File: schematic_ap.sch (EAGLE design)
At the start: 25 parts, among them M1 WIRELESS-NRF24L01, U1 ATMEGA328P_TQFP, U3 MPU-6050

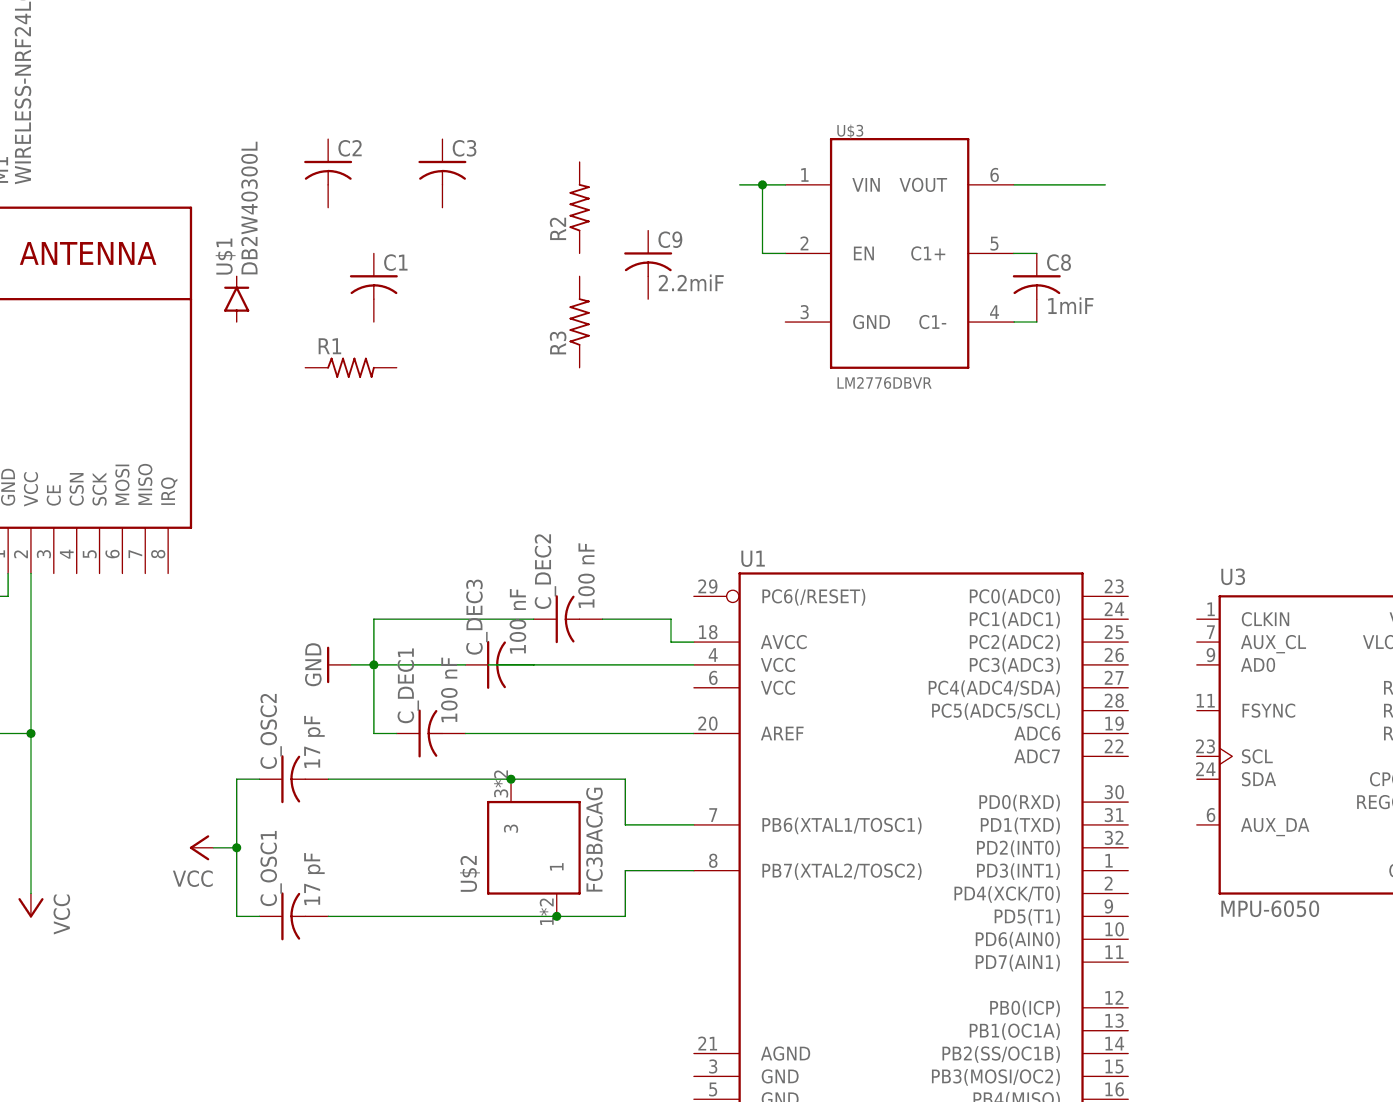
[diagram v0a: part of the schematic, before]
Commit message: New Oscillator
Added the 8MHZ Oscillator
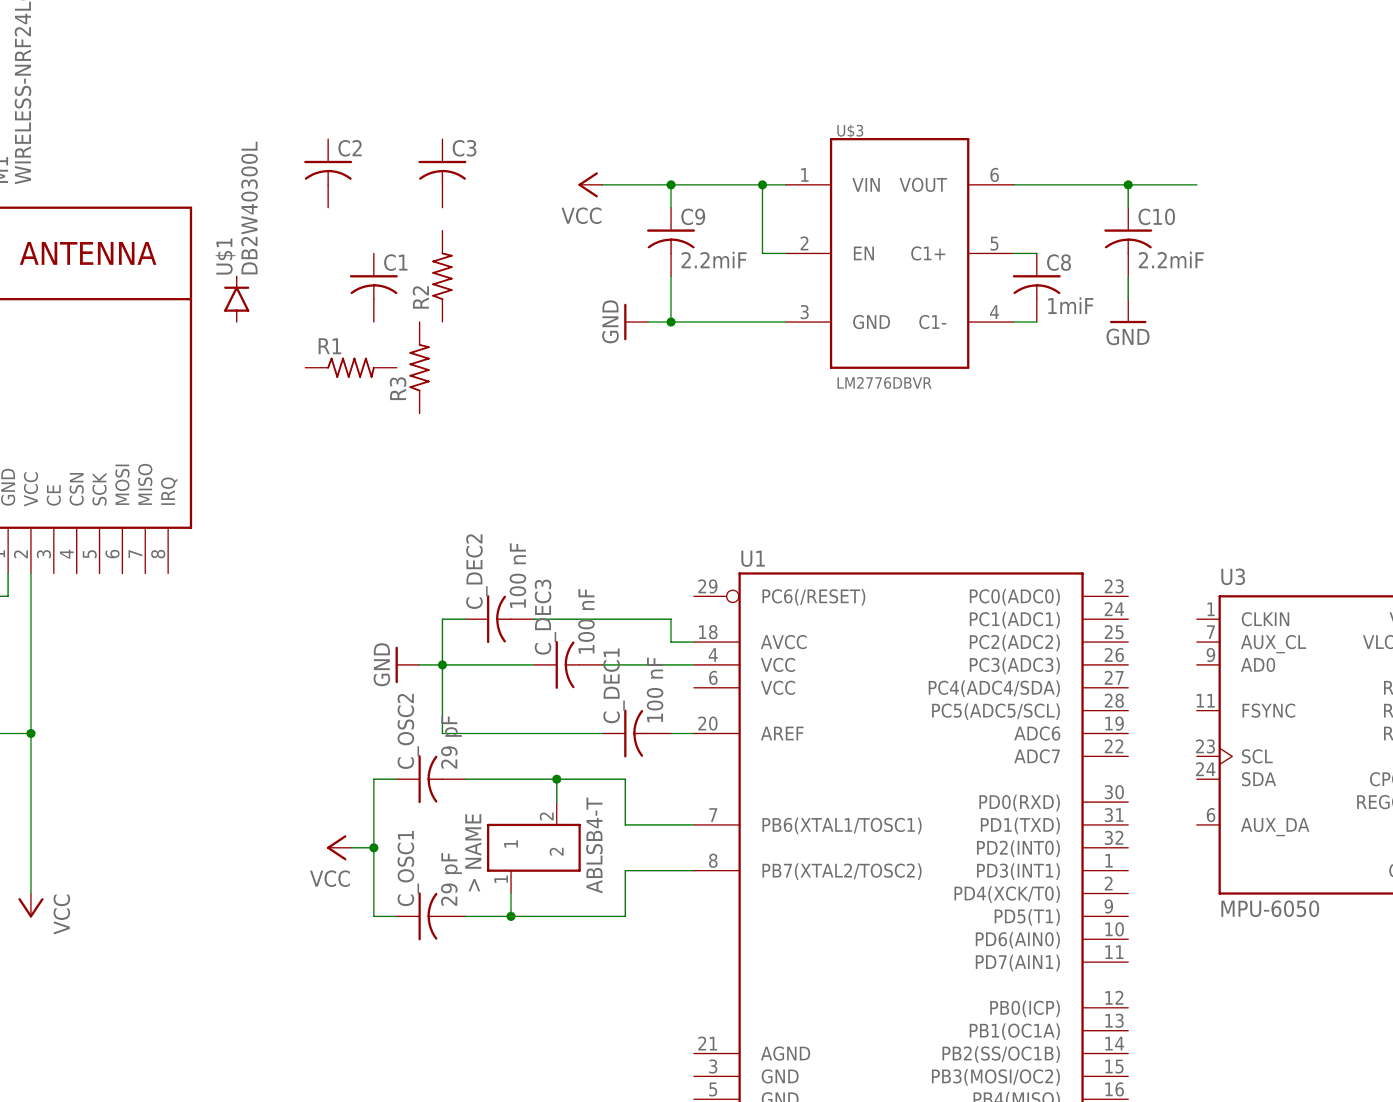
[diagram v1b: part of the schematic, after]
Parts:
- removed U$2: FC3BACAG, FC3BACAG:FC3BACAG
- added C10: 2.2miF, rcl:C-USC0603
- added OSC_8MHZ: ABLSB4-T, ABLS_B4_T:ABLSB4-T
- C_OSC1, C_OSC2: value 17 pF -> 29 pF
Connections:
- removed net N$15: U$3.EN, U$3.VIN
- net GND: now also C10.2, C9.2, U$3.GND
- net N$10: now also OSC_8MHZ.1; no longer U$2.1
- net N$14: now also C10.1
- net N$9: now also OSC_8MHZ.2; no longer U$2.3
- net VCC: now also C9.1, U$3.EN, U$3.VIN
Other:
- moved on the sheet: C9, C_DEC1, C_DEC2, C_DEC3, C_OSC1, C_OSC2, R2, R3

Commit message: More wiring
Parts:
- removed U$1: DB2W40300L, quad:DB2W40300L
- added D1, D2: RED, LEDs:LED-RED0603
- added D3, D4: GREEN, LEDs:LED-GREEN0603
- added D_M1: DB2W40300L, quad:DB2W40300L
- added R4, R5, R6: (no value), resistor:R-US_R0603
- added R_M1: 10 kΩ, resistor:R-US_R0603
- added U$2: 2N7002P, 2N7002P:2N7002P
- added U$4: JST_CONNECTOR_FEMALE, quad:JST_CONNECTOR_FEMALE
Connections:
- new net N$11: R_M1.2, U$2.S
- new net N$15: D_M1.PPIN, U$2.D, U$4.-
- new net N$16: U1.PC5(ADC5/SCL), U3.SCL
- new net N$17: U1.PC4(ADC4/SDA), U3.SDA
- new net N$18: D4.A, U1.PD0(RXD)
- new net N$19: D4.C, R4.2
- new net N$20: D2.A, U1.PD2(INT0)
- new net N$21: D2.C, R5.2
- new net N$22: D3.A, U1.PD1(TXD)
- new net N$23: D3.C, R6.2
- new net N$24: M1.CSN, U1.PB2(SS/OC1B)
- new net N$25: M1.MOSI, U1.PB3(MOSI/OC2)
- new net N$26: M1.MISO, U1.PB4(MISO)
- new net N$27: M1.SCK, U1.PB5(SCK)
- new net N$29: M1.CE, U1.ADC6
- net GND: now also R4.1, R5.1, R6.1, R_M1.1
- net VCC: now also D_M1.GPIN, U$4.+
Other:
- moved on the sheet: C4, C5, C6, C7, C_R1, C_R2, M1, U3

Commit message: Schematic Wiring
Wiring of parts
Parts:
- removed R4, R5, R6: (no value), resistor:R-US_R0603
- added D_M2, D_M3, D_M4: DB2W40300L, quad:DB2W40300L
- added J1: FTDI_DEVICE, quad:FTDI_DEVICE
- added R_LED1, R_LED2, R_LED3, R_LED4: 150 Ω, resistor:R-US_R0603
- added R_M2, R_M3, R_M4: 10 kΩ, resistor:R-US_R0603
- added U$1, U$6, U$8: 2N7002P, 2N7002P:2N7002P
- added U$5, U$7, U$9: JST_CONNECTOR_FEMALE, quad:JST_CONNECTOR_FEMALE
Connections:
- net N$1 renamed AVCC
- net N$10 renamed TOSC2
- net N$16 renamed SCL
- net N$17 renamed SDA
- net N$22 renamed PD1
- net N$24 renamed CSN
- net N$25 renamed MOSI
- net N$26 renamed MISO
- net N$27 renamed SCK
- net N$29 renamed CE
- net N$4 renamed AREF
- net N$9 renamed TOSC1
- removed net N$3: C_DEC3.2, U1.VCC@4
- removed net N$7: C5.2, U3.VDD
- removed net N$8: C7.2, U3.VLOGIC
- new net N$22: R_M3.2, U$6.S
- new net N$24: D_M3.PPIN, U$6.D, U$7.-
- new net N$25: R_M4.2, U$8.S
- new net N$26: D_M4.PPIN, U$8.D, U$9.-
- new net N$30: D1.C, R_LED1.2
- new net PB0: D1.A, U1.PB0(ICP)
- new net PB1: U$2.G, U1.PB1(OC1A)
- new net PD0: D2.A, U1.PD0(RXD)
- new net PD2: D4.A, U1.PD2(INT0)
- new net PD3: U$1.G, U1.PD3(INT1)
- new net PD5: U$6.G, U1.PD5(T1)
- new net PD6: U$8.G, U1.PD6(AIN0)
- new net RESET: U1.PC6(/RESET)
- net GND: now also R_LED1.1, R_LED2.1, R_LED3.1, R_LED4.1, R_M2.1, R_M3.1, R_M4.1, U3.GND; no longer R4.1, R5.1, R6.1
- net N$18: now also R_M2.2, U$1.S; no longer D4.A, U1.PD0(RXD)
- net N$19: now also R_LED4.2; no longer R4.2
- net N$20: now also D_M2.PPIN, U$1.D, U$5.-; no longer D2.A, U1.PD2(INT0)
- net N$21: now also R_LED2.2; no longer R5.2
- net N$23: now also R_LED3.2; no longer R6.2
- net VCC: now also C5.2, C7.2, C_DEC3.2, D_M2.GPIN, D_M3.GPIN, D_M4.GPIN, U$5.+, U$7.+, U$9.+, U1.VCC@4, U3.VDD, U3.VLOGIC
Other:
- moved on the sheet: C4, C5, C6, C7, C_DEC1, C_DEC2, C_DEC3, C_OSC1, C_OSC2, C_R1, C_R2, D1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

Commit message: Pre-Schematic Review Finalized Version
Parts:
- removed C1: (no value), rcl:C-USC0603
- removed C10, C9: 2.2miF, rcl:C-USC0603
- removed C2: (no value), rcl:C-USC0402
- removed C3: (no value), rcl:C-USC0805
- removed C4, C5, C_R2: 100 nF, rcl:C-USC0603
- removed C6: 2.2 nF, rcl:C-USC0603
- removed C7: 10 nF, rcl:C-USC0603
- removed C8: 1miF, rcl:C-USC0603
- removed C_R1: 100 miF, rcl:C-USC0603
- removed R1, R2, R3: (no value), resistor:R-US_R0603
- added C_BAT: 100 miF, rcl:C-USC0805
- added C_CP1: 1miF, rcl:C-USC0603
- added C_CP2, C_CP3: 2.2miF, rcl:C-USC0603
- added C_G1, C_G4, C_R, C_RF2: 100 nF, rcl:C-USC0603
- added C_G2: 10 nF, rcl:C-USC0603
- added C_G3: 2.2 nF, rcl:C-USC0603
- added C_RF1: 100 miF, rcl:C-USC0603
- added R5: 6.6 kΩ, resistor:R-US_R0603
- added R_VD1, R_VD2: 100 kΩ, resistor:R-US_R0603
- added U$10: PTS645, PTS645:PTS645
- added U$11: JST_CONNECTOR_FEMALE, quad:JST_CONNECTOR_FEMALE
- C_OSC1, C_OSC2: value 29 pF -> 30 pF
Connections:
- net PB0 renamed D_OUT1
- net PD2 renamed D_OUT4
- removed net N$14: C10.1, U$3.VOUT
- removed net PB1: U$2.G, U1.PB1(OC1A)
- removed net PD0: D2.A, U1.PD0(RXD)
- removed net PD1: D3.A, U1.PD1(TXD)
- removed net PD3: U$1.G, U1.PD3(INT1)
- removed net PD5: U$6.G, U1.PD5(T1)
- removed net PD6: U$8.G, U1.PD6(AIN0)
- removed net VCC: C5.2, C7.2, C9.1, C_DEC3.2, C_OSC1.1, C_OSC2.1, C_R1.2, C_R2.2, D_M1.GPIN, D_M2.GPIN, D_M3.GPIN, D_M4.GPIN, M1.VCC, U$3.EN, U$3.VIN, U$4.+, U$5.+, U$7.+, U$9.+, U1.VCC@4, U3.VDD, U3.VLOGIC
- new net B_OUT: C_BAT.1, C_CP2.1, D_M1.GPIN, D_M2.GPIN, D_M3.GPIN, D_M4.GPIN, R_VD2.2, U$11.+, U$3.EN, U$3.VIN, U$4.+, U$5.+, U$7.+, U$9.+
- new net D_OUT2: D2.A, U1.PC0(ADC0)
- new net D_OUT3: D3.A, U1.PC1(ADC1)
- new net N$3: C_R.1, J1.DTR
- new net N$7: R_VD1.2, R_VD2.1
- new net PWM1: U$2.G, U1.PD3(INT1)
- new net PWM2: U$1.G, U1.PD5(T1)
- new net PWM3: U$6.G, U1.PD6(AIN0)
- new net PWM4: U$8.G, U1.PB1(OC1A)
- new net P_OUT: C_CP3.1, C_DEC3.1, C_G1.1, C_G2.1, C_OSC1.1, C_OSC2.1, C_RF1.1, C_RF2.1, J1.VCC, M1.VCC, R5.1, U$3.VOUT, U1.VCC@4, U1.VCC@6, U3.VDD, U3.VLOGIC
- new net RX/TX: J1.TXO, U1.PD0(RXD)
- new net TX/RX: J1.RXI, U1.PD1(TXD)
- net AREF: now also C_DEC1.1; no longer C_DEC1.2
- net AVCC: now also C_DEC2.1; no longer C_DEC2.2
- net GND: now also C_BAT.2, C_CP2.2, C_CP3.2, C_DEC1.2, C_DEC2.2, C_DEC3.2, C_G1.2, C_G2.2, C_G3.2, C_G4.2, J1.GND, R_VD1.1, U$10.1, U$11.-; no longer C10.2, C4.1, C5.1, C6.1, C7.1, C9.2, C_DEC1.1, C_DEC2.1, C_DEC3.1
- net N$12: now also C_CP1.1; no longer C8.1
- net N$13: now also C_CP1.2; no longer C8.2
- net N$2: now also C_RF1.2, C_RF2.2; no longer C_R1.1, C_R2.1
- net N$5: now also C_G3.1; no longer C6.2
- net N$6: now also C_G4.1; no longer C4.2
- net RESET: now also C_R.2, R5.2, U$10.3
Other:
- moved on the sheet: C_DEC1, C_DEC2, C_DEC3, C_OSC1, C_OSC2, D1, D2, D3, D4, D_M1, D_M2, D_M3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

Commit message: Actual Pre-Schematic Review Finalized Version
Foooo real
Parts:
- R5: value 6.6 kΩ -> 7 kΩ
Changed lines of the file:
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@@
 <part name="GND14" library="supply1" library_urn="urn:adsk.eagle:library:371" deviceset="GND" device=""/>
 <part name="GND15" library="supply1" library_urn="urn:adsk.eagle:library:371" deviceset="GND" device=""/>
-<part name="R5" library="resistor" library_urn="urn:adsk.eagle:library:348" deviceset="R-US_" device="R0603" package3d_urn="urn:adsk.eagle:package:26057/1" value="6.6 kΩ"/>
+<part name="R5" library="resistor" library_urn="urn:adsk.eagle:library:348" deviceset="R-US_" device="R0603" package3d_urn="urn:adsk.eagle:package:26057/1" value="7 kΩ"/>
 <part name="C_R" library="rcl" library_urn="urn:adsk.eagle:library:334" deviceset="C-US" device="C0603" package3d_urn="urn:adsk.eagle:package:23616/2" value="100 nF"/>
 <part name="C_BAT" library="rcl" library_urn="urn:adsk.eagle:library:334" deviceset="C-US" device="C0805" package3d_urn="urn:adsk.eagle:package:23617/2" value="100 miF"/>
